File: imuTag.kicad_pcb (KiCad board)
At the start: 4 copper layers, 41.3 x 40 mm, 45 parts, among them J1 Conn_02x05_Odd_Even, J2 Conn_01x05_Socket, J3 Conn_01x02_Pin, U1 E73-2G4M08S1C, U2 ME6211C30M5G-N, U3 GD25Q64ESIG, U4 LSM6DSV16XTR, U5 LIS2MDLTR, Y2 Crystal

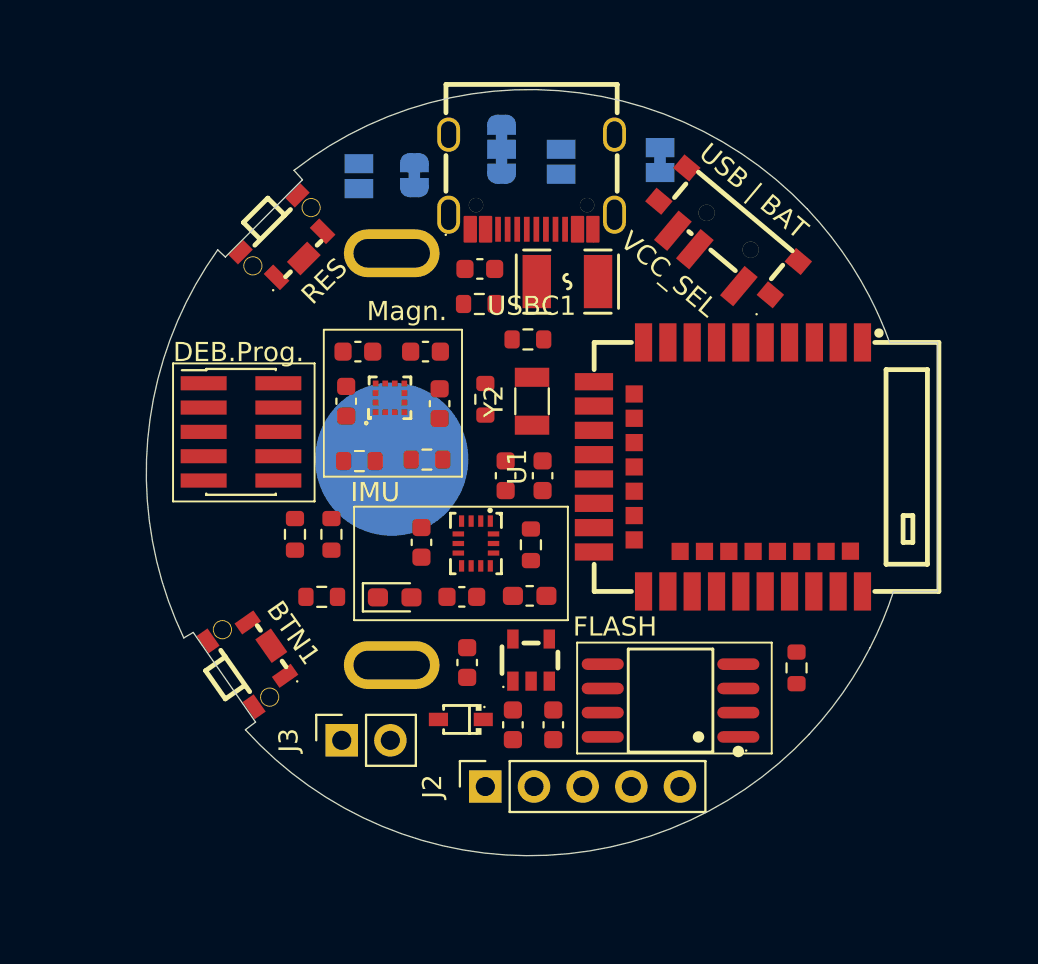
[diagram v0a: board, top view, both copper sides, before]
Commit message: Add copper zones before routing
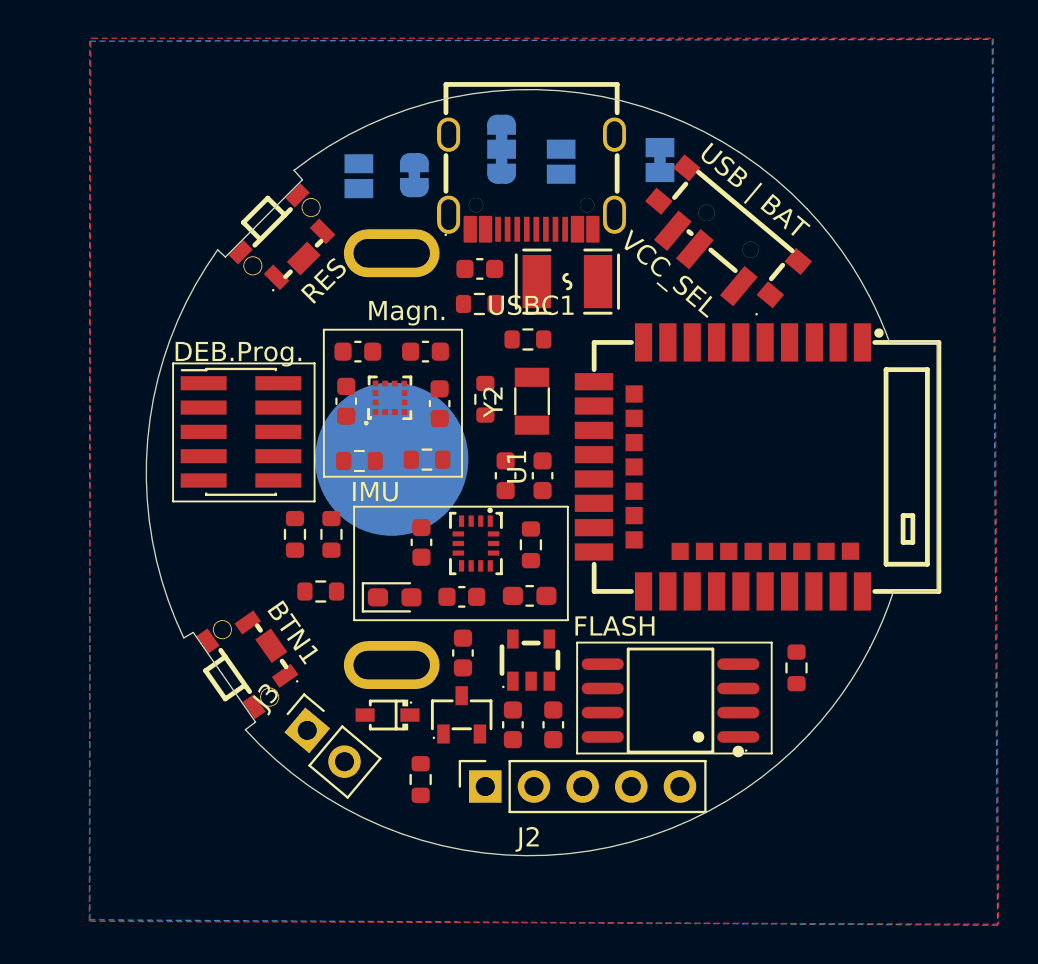
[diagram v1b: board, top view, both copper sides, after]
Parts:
- added Q1: DMG2305UX-13, EasyEDA:SOT-23-3_L2.9-W1.3-P1.90-LS2.4-BR, F.Cu at (165.9, 112.8)
- added R6: 100K, Resistor_SMD:R_0603_1608Metric, F.Cu at (163.8, 116.1)
- moved D3 3.84 mm to (162.1, 112.8)
- moved J3 1.87 mm to (157.9, 113.6), turned to 50 degrees
- moved C3 0.54 mm to (166.0, 109.5)
- moved R5 0.28 mm to (158.6, 106.3)
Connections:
- BAT1 pad 1: /VBAT -> Net-(Q1-D)
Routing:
- added copper zone on In1.Cu, net (none)
- added copper zone on In2.Cu, net /+5V_USB
- added copper zone on F.Cu, net /VBAT
- added copper zone on In2.Cu, net /VBAT
- added copper zone on B.Cu, net GND
- added copper zone on In2.Cu, net VCC

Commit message: Save current routing work
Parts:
- removed JP6: SolderJumper_3_Bridged123, Jumper:SolderJumper-3_P1.3mm_Bridged123_RoundedPad1.0x1.5mm
- removed JP9: SolderJumper_2_Bridged, Jumper:SolderJumper-2_P1.3mm_Bridged_RoundedPad1.0x1.5mm
- moved J3 28.9 mm to (160.5, 84.8), turned to 120 degrees
- moved D3 25.3 mm to (174.9, 90.9)
- moved JP1 24.7 mm to (179.4, 100.6), turned to 180 degrees
- moved R6 23.0 mm to (163.6, 93.1), turned to 180 degrees
- moved C3 22.3 mm to (174.8, 89.1), turned to 180 degrees
- moved Q1 21.4 mm to (160.2, 92.1)
- moved JP7 21.1 mm to (184.1, 100.6), turned to 180 degrees
- moved C16 16.9 mm to (171.9, 111.9)
- moved C17 16.9 mm to (167.6, 109.1)
- moved R16 16.9 mm to (167.7, 114.9)
- moved R18 16.9 mm to (171.2, 114.8)
- moved U5 16.9 mm to (169.3, 111.6)
- moved C21 16.9 mm to (171.1, 109.1)
- moved C19 16.8 mm to (166.9, 111.6)
- moved U2 15.3 mm to (163.3, 96.0)
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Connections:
- net Net-(J3-Pin_1) renamed /VCC_1
- BAT1 pad 1: Net-(Q1-D) -> /VBAT
- Q1 pad 2: /VBAT -> /VBAT1
- Q1 pad 3: Net-(Q1-D) -> /VBAT
- R15 pad 2: Net-(JP9-A) -> Net-(JP7-B)
- R16 pad 1: Net-(JP6-B) -> VCC
- R18 pad 1: Net-(JP6-A) -> VCC
- U1 pad 16: /LIS2MDL_INT -> /LSM6DSV16_INT2
- U1 pad 17: unconnected-(U1-P1.09-Pad17) -> /LSM6DSV16_INT2
- U1 pad 38: /LSM6DSV16_INT2 -> /LIS2MDL_INT
- VCCSEL1 pad 1: /VBAT -> /VBAT1
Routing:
- net VCC: track 0.00 -> 70.7 mm, vias 0 -> 20
- net /+5V_USB: track 0.00 -> 36.8 mm, vias 0 -> 3
- net GND: track 0.00 -> 36.4 mm, vias 0 -> 17
- net /USB_D+: track 0.00 -> 32.2 mm, vias 0 -> 2
- net /USB_D-: track 0.00 -> 29.8 mm, vias 0 -> 2
- net /VCC_1: track 0.00 -> 24.9 mm, vias 0 -> 3
- net /VBAT1: track 0.00 -> 22.0 mm, vias 0 -> 2
- net Net-(D3-K): track 0.00 -> 18.6 mm, vias 0 -> 2
- net /QSPI_IO2: track 0.00 -> 14.6 mm, vias 0 -> 2
- net /QSPI_IO0: track 0.00 -> 13.7 mm, vias 0 -> 2
- net /QSPI_IO1: track 0.00 -> 13.3 mm, vias 0 -> 2
- net /USB_3V0: track 0.00 -> 9.07 mm
- net /QSPI_CS: track 0.00 -> 8.74 mm
- net /QSPI_CLK: track 0.00 -> 7.65 mm
- net /QSPI_IO3: track 0.00 -> 6.40 mm
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- added copper zone on F.Cu, net GND
- added copper zone on In1.Cu, net GND
- removed copper zone on In1.Cu, net (none)
- removed copper zone on F.Cu, net /VBAT
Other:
- board text removed: "VCC_SEL"

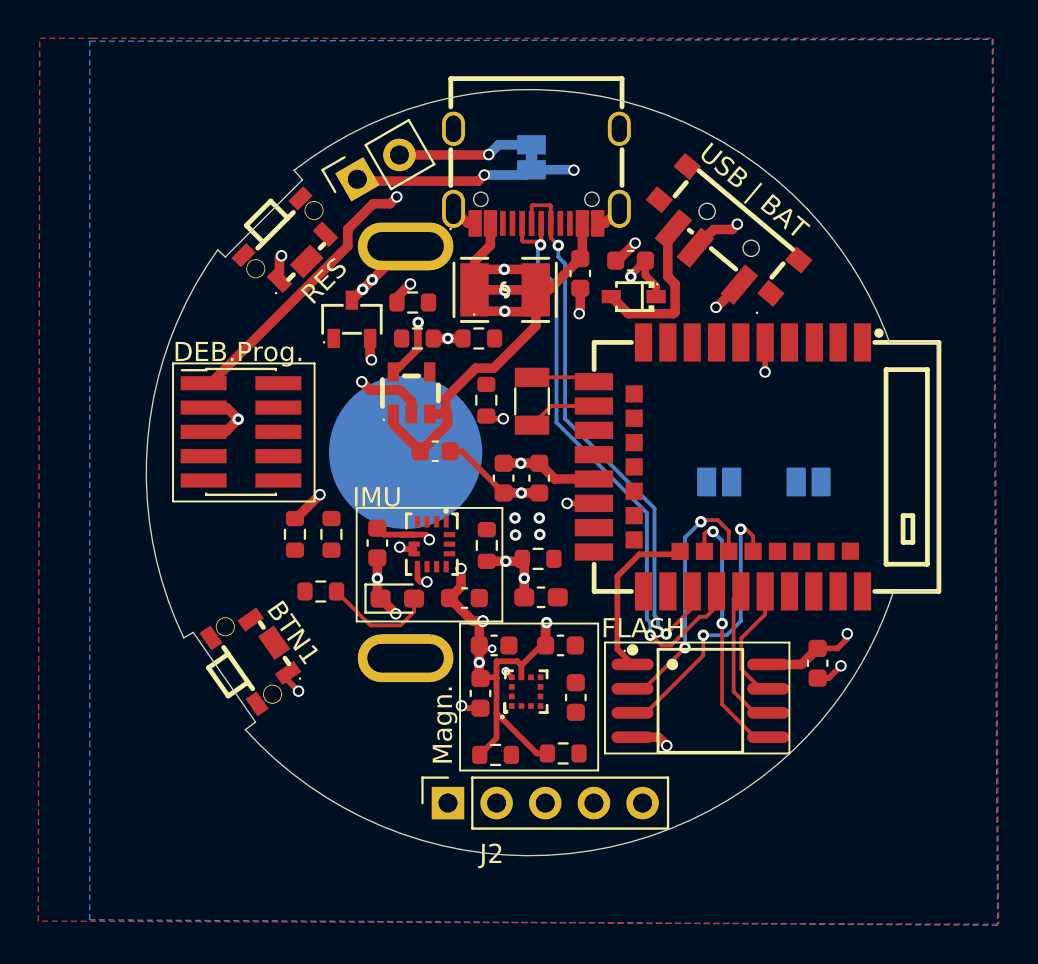
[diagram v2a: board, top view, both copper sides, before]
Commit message: draw Important Tracks
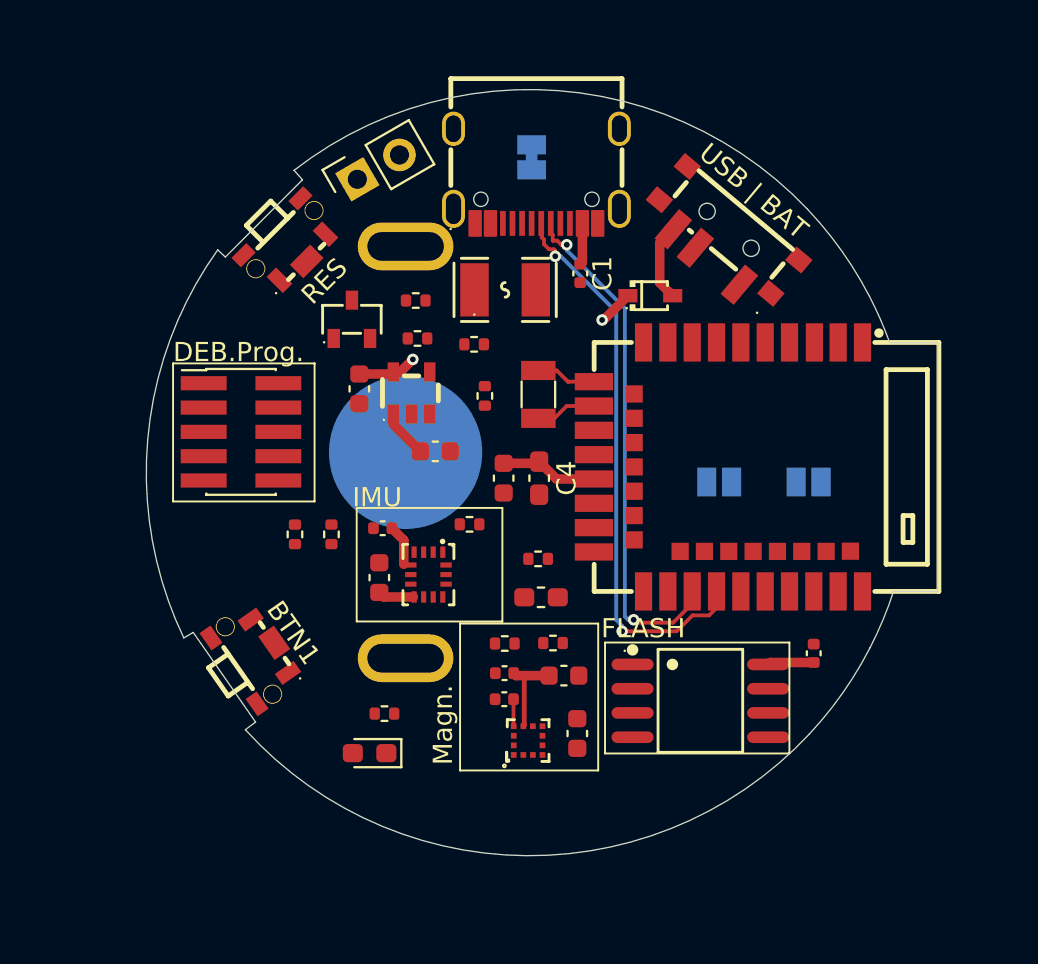
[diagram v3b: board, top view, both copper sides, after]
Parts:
- removed J2: Conn_01x05_Socket, Connector_PinSocket_2.54mm:PinSocket_1x05_P2.54mm_Vertical
- C1, C14, C17, C19, C20: footprint Capacitor_SMD:C_0603_1608Metric -> Capacitor_SMD:C_0402_1005Metric
- C4: footprint Capacitor_SMD:C_0603_1608Metric -> Capacitor_SMD:C_0603_1608Metric_Pad1.08x0.95mm_HandSolder
- R1, R10, R11, R15, R16, R18, R2, R3, R4, R5, R6: footprint Resistor_SMD:R_0603_1608Metric -> Resistor_SMD:R_0402_1005Metric
- moved C3 15.7 mm to (160.6, 95.7), turned to -90 degrees
- moved D2 8.20 mm to (161.1, 114.8), turned to 180 degrees
- moved R5 7.19 mm to (161.9, 112.7), turned to 180 degrees
- moved R16 5.84 mm to (168.2, 109.0), turned to 180 degrees
- moved R18 5.79 mm to (170.7, 109.0)
- moved C20 5.62 mm to (161.8, 103.0), turned to 180 degrees
- moved C17 2.86 mm to (168.2, 112.0), turned to 0 degrees
- moved U5 2.55 mm to (169.4, 114.1)
- moved C16 1.88 mm to (172.0, 113.7)
- moved C18 1.81 mm to (161.6, 105.6), turned to 90 degrees
- moved C19 1.64 mm to (168.2, 110.6), turned to 0 degrees
- moved U4 1.60 mm to (164.2, 105.4)
- moved C21 1.58 mm to (171.3, 110.7)
- moved R10 1.43 mm to (166.4, 102.8), turned to 0 degrees
- moved D3 0.87 mm to (175.8, 90.9), turned to 0 degrees
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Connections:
- U1 pad 10: /AI6 -> unconnected-(U1-AI6-Pad10)
- U1 pad 4: /AI4 -> unconnected-(U1-AI4-Pad4)
- U1 pad 7: /AI0 -> unconnected-(U1-AI0-Pad7)
- U1 pad 8: /AI5 -> unconnected-(U1-AI5-Pad8)
- U1 pad 9: /AI7 -> unconnected-(U1-AI7-Pad9)
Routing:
- net VCC: track 70.7 -> 17.5 mm, vias 20 -> 0
- net GND: track 36.4 -> 0.00 mm, vias 17 -> 0
- net /+5V_USB: track 36.8 -> 4.71 mm, vias 3 -> 0
- net /VCC_1: track 24.9 -> 0.00 mm, vias 3 -> 0
- net /VBAT1: track 22.0 -> 0.00 mm, vias 2 -> 0
- net /QSPI_IO2: track 14.6 -> 0.00 mm, vias 2 -> 0
- net /QSPI_IO0: track 13.7 -> 0.00 mm, vias 2 -> 0
- net /QSPI_IO1: track 13.3 -> 0.00 mm, vias 2 -> 0
- net /QSPI_CS: track 8.74 -> 0.00 mm
- net /QSPI_CLK: track 7.65 -> 0.00 mm
- net /QSPI_IO3: track 6.40 -> 0.00 mm
- net /VBAT: track 5.79 -> 0.00 mm, vias 3 -> 0
- net Net-(D2-A): track 5.76 -> 0.00 mm
- net /USB_3V0: track 9.07 -> 4.04 mm
- net Net-(D3-K): track 18.6 -> 15.7 mm
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- removed copper zone on In2.Cu, net /+5V_USB
- removed copper zone on In2.Cu, net /VBAT
- removed copper zone on B.Cu, net GND
- removed copper zone on F.Cu, net GND
- removed copper zone on In1.Cu, net GND
- removed copper zone on In2.Cu, net VCC

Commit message: Add autorouted PCB layout
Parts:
- moved C1 1.50 mm to (173.5, 89.2), turned to 0 degrees
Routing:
- net /RESET: track 0.00 -> 47.1 mm, vias 0 -> 3
- net /USB_D+: track 29.6 -> 71.1 mm
- net Net-(JP7-B): track 0.00 -> 40.8 mm, vias 0 -> 4
- net /SWDIO: track 0.00 -> 38.5 mm, vias 0 -> 2
- net /SWDCLK: track 0.00 -> 37.5 mm, vias 0 -> 2
- net /I2C0_SCL: track 0.00 -> 37.0 mm, vias 0 -> 2
- net /SPI1_SCLK: track 0.00 -> 36.2 mm, vias 0 -> 2
- net /SPI1_MOSI: track 0.00 -> 34.3 mm, vias 0 -> 2
- net /LSM6DSV16_INT1: track 0.00 -> 33.2 mm, vias 0 -> 2
- net /USB_D-: track 27.1 -> 59.8 mm
- net /VBAT: track 0.00 -> 32.6 mm
- net /LSM6DSV16_CS: track 0.00 -> 31.8 mm, vias 0 -> 2
- net /I2C0_SDA: track 0.00 -> 29.4 mm, vias 0 -> 2
- net /BTN1: track 0.00 -> 27.1 mm, vias 0 -> 2
- net /SPI1_MISO: track 0.00 -> 25.9 mm, vias 0 -> 2
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
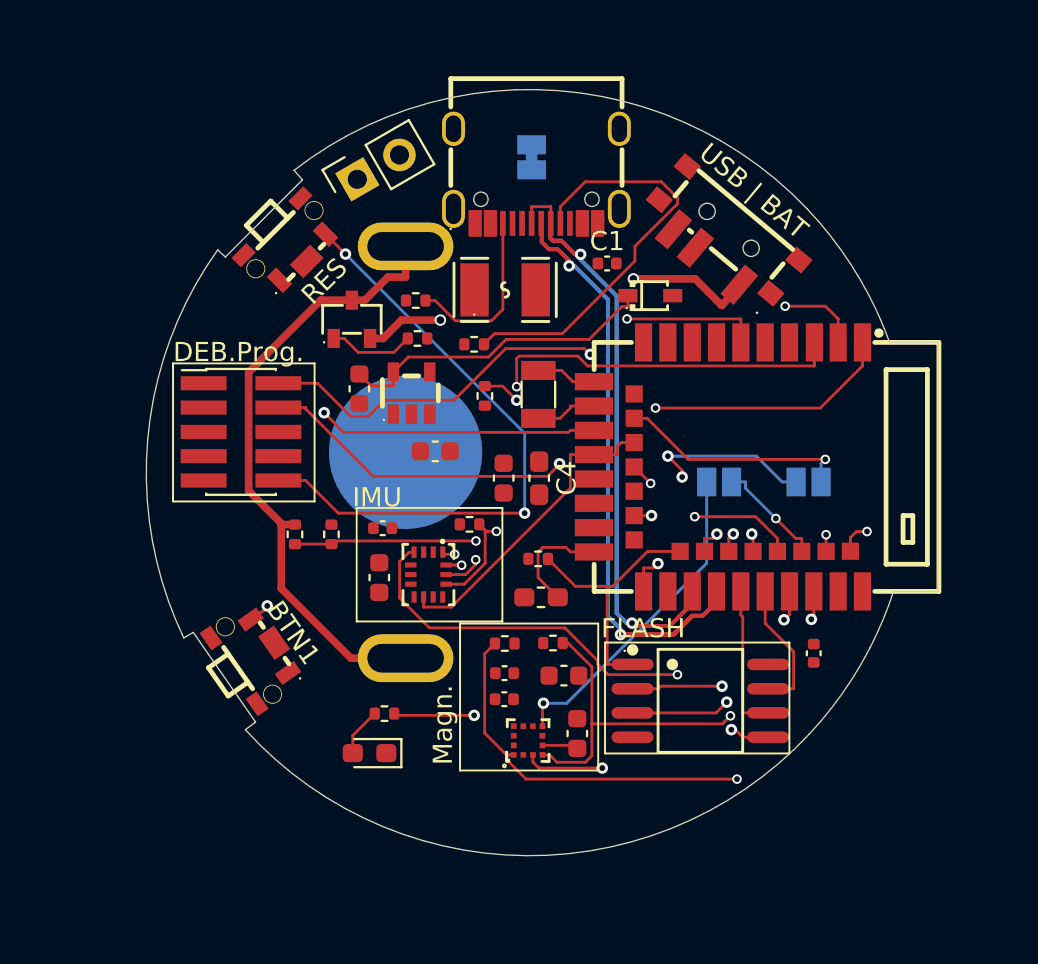
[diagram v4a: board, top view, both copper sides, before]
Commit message: Complete routed PCB layout
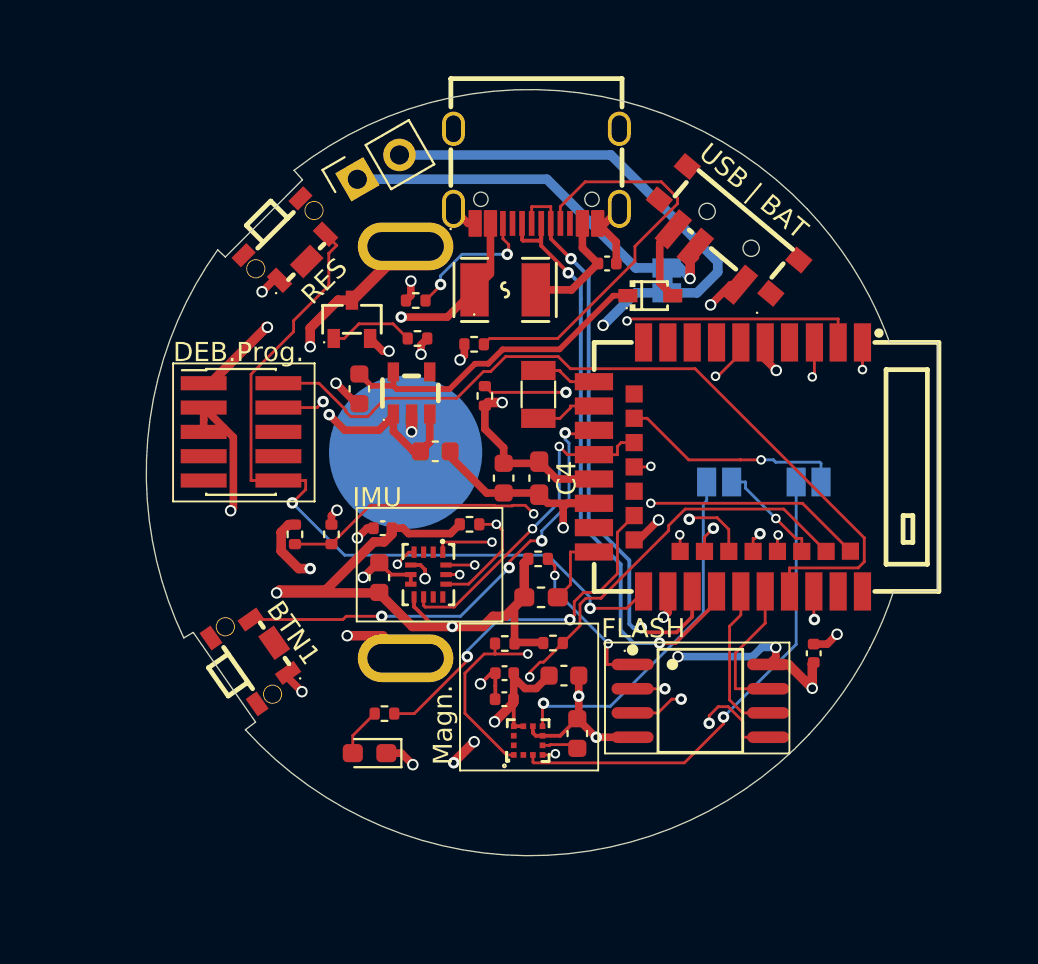
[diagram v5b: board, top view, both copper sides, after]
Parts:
- moved JP2 9.55 mm to (176.7, 90.1), turned to 90 degrees
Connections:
- C1 pad 1: /+5V_USB -> /+5V_USB_prot
- F1 pad 2: /+5V_USB -> /+5V_USB_prot
- USBC1 pad A4B9: /+5V_USB -> /+5V_USB_prot
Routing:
- net VCC: track 0.00 -> 173.1 mm, vias 0 -> 13
- net GND: track 0.00 -> 55.5 mm, vias 0 -> 19
- net /USB_D+: track 71.1 -> 33.0 mm
- net /USB_D-: track 59.8 -> 32.0 mm
- net /+5V_USB: track 0.00 -> 24.2 mm, vias 0 -> 2
- net /VCC_1: track 0.00 -> 21.3 mm, vias 0 -> 1
- net Net-(JP7-B): track 40.8 -> 50.9 mm, vias 4 -> 2
- net /LSM6DSV16_INT1: track 33.2 -> 42.0 mm
- net /RESET: track 47.1 -> 40.6 mm, vias 3 -> 2
- net /+5V_USB_prot: track 0.00 -> 6.24 mm
- net /I2C0_SCL: track 37.0 -> 31.8 mm
- net /SWDCLK: track 37.5 -> 42.4 mm
- net /SWDIO: track 38.5 -> 43.1 mm, vias 2 -> 0
- net /SPI1_SCLK: track 36.2 -> 32.0 mm
- net /USB_3V0: track 0.00 -> 4.04 mm
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- added copper zone on In1.Cu, net GND

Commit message: Finalize PCB for production
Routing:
- net GND: track 55.5 -> 61.2 mm, vias 19 -> 18
- net /SWDIO: track 43.1 -> 42.0 mm, vias 0 -> 2
- net /+5V_USB: track 24.2 -> 24.7 mm
- added copper zone on B.Cu, net GND
- added copper zone on F.Cu, net GND
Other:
- board text added: "Bauer Labs IMU-TAG: A-1.0"
- board text added: "C2032"
- board text added: "Cut for current measurement"
- board text added: "LED"
- board text added: "LIS2MDL SPI Option"
